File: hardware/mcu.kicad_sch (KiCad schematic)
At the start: 61 parts, among them J1 TYPE-C 16PIN 2MD(073), J2 Conn_ARM_JTAG_SWD_10, J22 Conn_01x16, J3 Conn_02x03_Odd_Even, J4 Conn_02x04_Odd_Even, Q1 DMP1045U-7, Q4 SS8050, Q5 SL1254-3, SW1 MK-12C01-G1.5, SW2 TS-1095PS-A1B2-C3D2, SW3 TS-1095PS-A1B2-C3D2, SW4 10*10*9-6P WX, U1 TPS63031DSK, U10 PY25Q128HA, U2 RP2350A-QFN60, U7 24CS02, Y1 12Mhz

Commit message: prototype v0.3
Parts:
- removed SW4: 10*10*9-6P WX, easyeda2kicad:SW-SMD-6P-L10.5-W10.0_C2858290, symbol easyeda2kicad:10*10*9-6PWX
- added SW5: 7*7*5-6P-L WX, easyeda2kicad:SW-SMD_8P-L7.0-W7.0-P1.40-LS7.4-TL, symbol easyeda2kicad:7*7*5-6P-LWX
- added TP4, TP5: TestPoint, TestPoint:TestPoint_Pad_D1.0mm, symbol Connector:TestPoint
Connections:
- net GND: now also SW5.2 (Public), TP4.1
- net JOY_B: now also U2.33 (GPIO21), SW5.5 (F1); no longer U2.31 (GPIO19)
- net JOY_D: now also SW5.4 (F5)
- net JOY_L: now also U2.31 (GPIO19), SW5.3 (F4); no longer U2.35 (GPIO23)
- net JOY_R: now also SW5.6 (F3)
- net JOY_U: now also U2.35 (GPIO23), SW5.1 (F2); no longer U2.33 (GPIO21)
- net at U2.43 (GPIO29_ADC3): now also TP5.1
- no-connect marks 15 -> 17

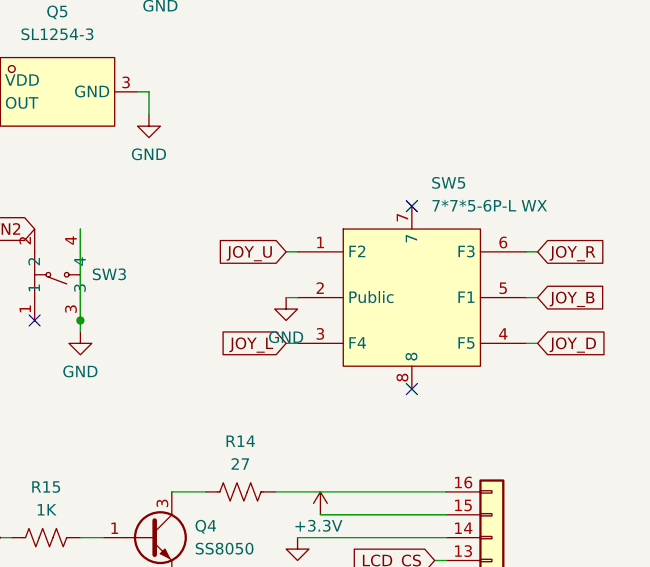
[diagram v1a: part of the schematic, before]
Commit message: Updated joystick
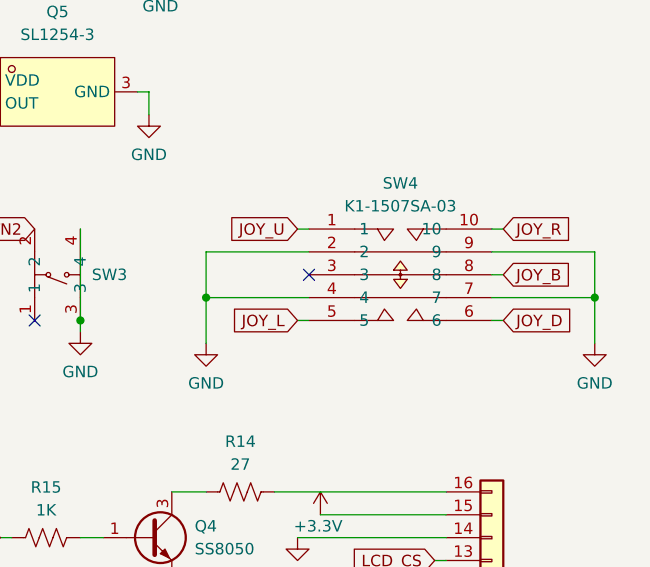
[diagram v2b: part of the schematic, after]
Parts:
- removed SW5: 7*7*5-6P-L WX, easyeda2kicad:SW-SMD_8P-L7.0-W7.0-P1.40-LS7.4-TL, symbol easyeda2kicad:7*7*5-6P-LWX
- added SW4: K1-1507SA-03, easyeda2kicad:KEY-SMD_K1-1507SA-03, symbol easyeda2kicad:K1-1507SA-03
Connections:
- net GND: now also SW4.2, SW4.4, SW4.7, SW4.9
- net JOY_B: now also SW4.8
- net JOY_D: now also SW4.6
- net JOY_L: now also SW4.5
- net JOY_R: now also SW4.10
- net JOY_U: now also SW4.1
- no-connect marks 17 -> 16

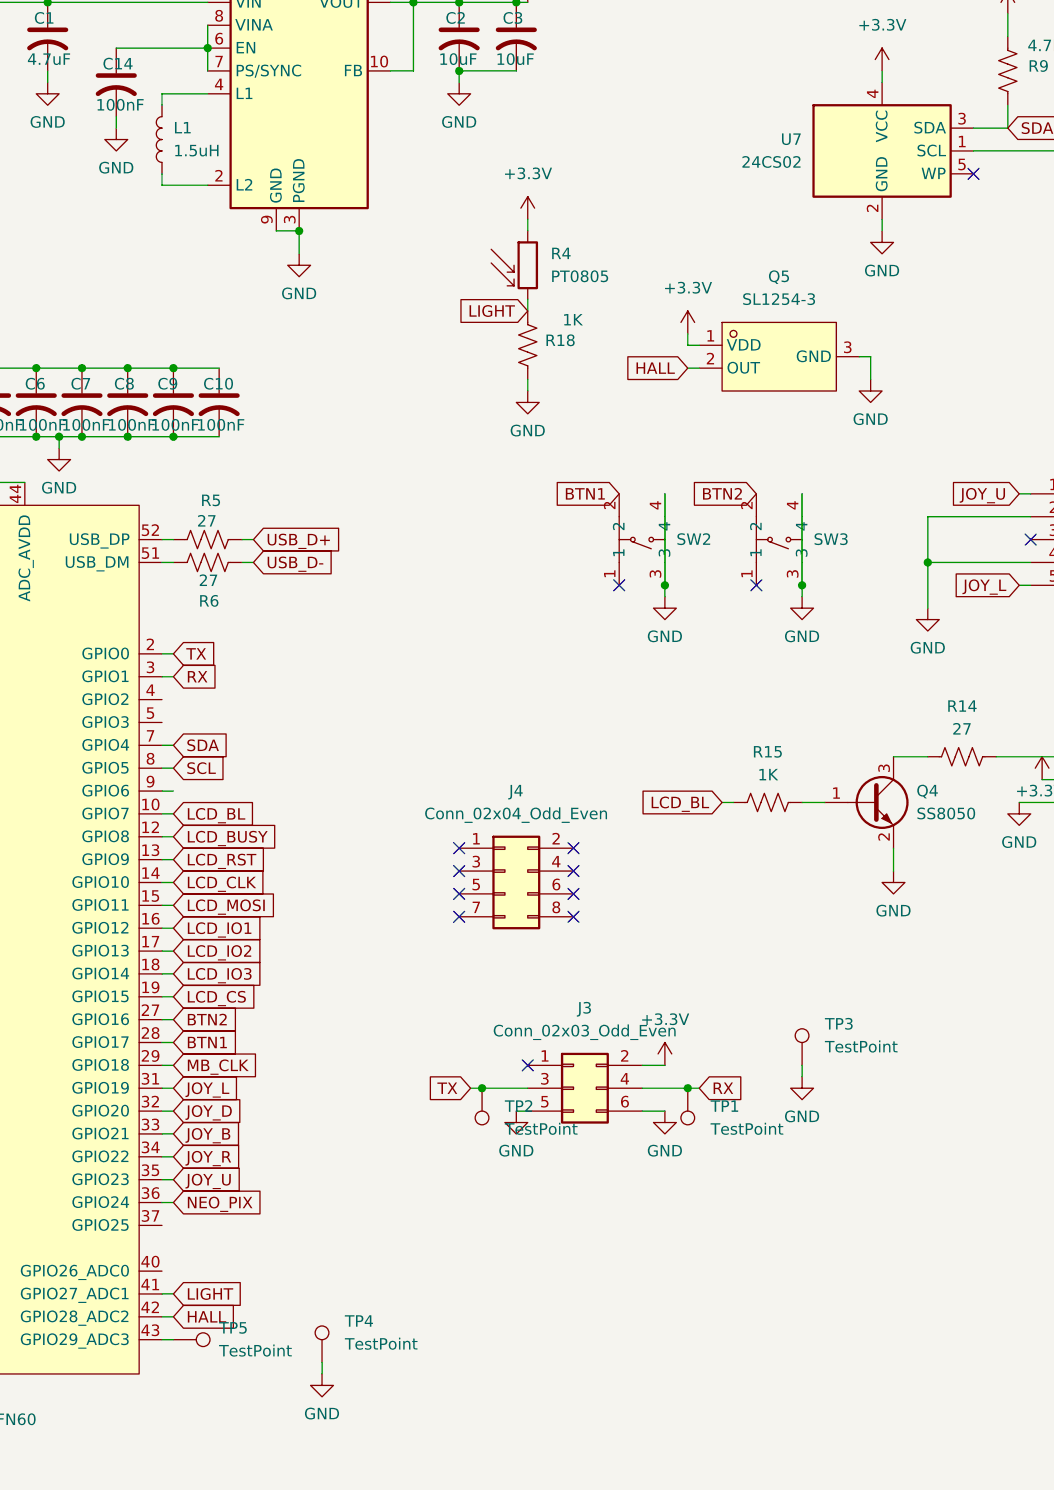
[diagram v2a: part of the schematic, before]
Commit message: Restoring Orion trail
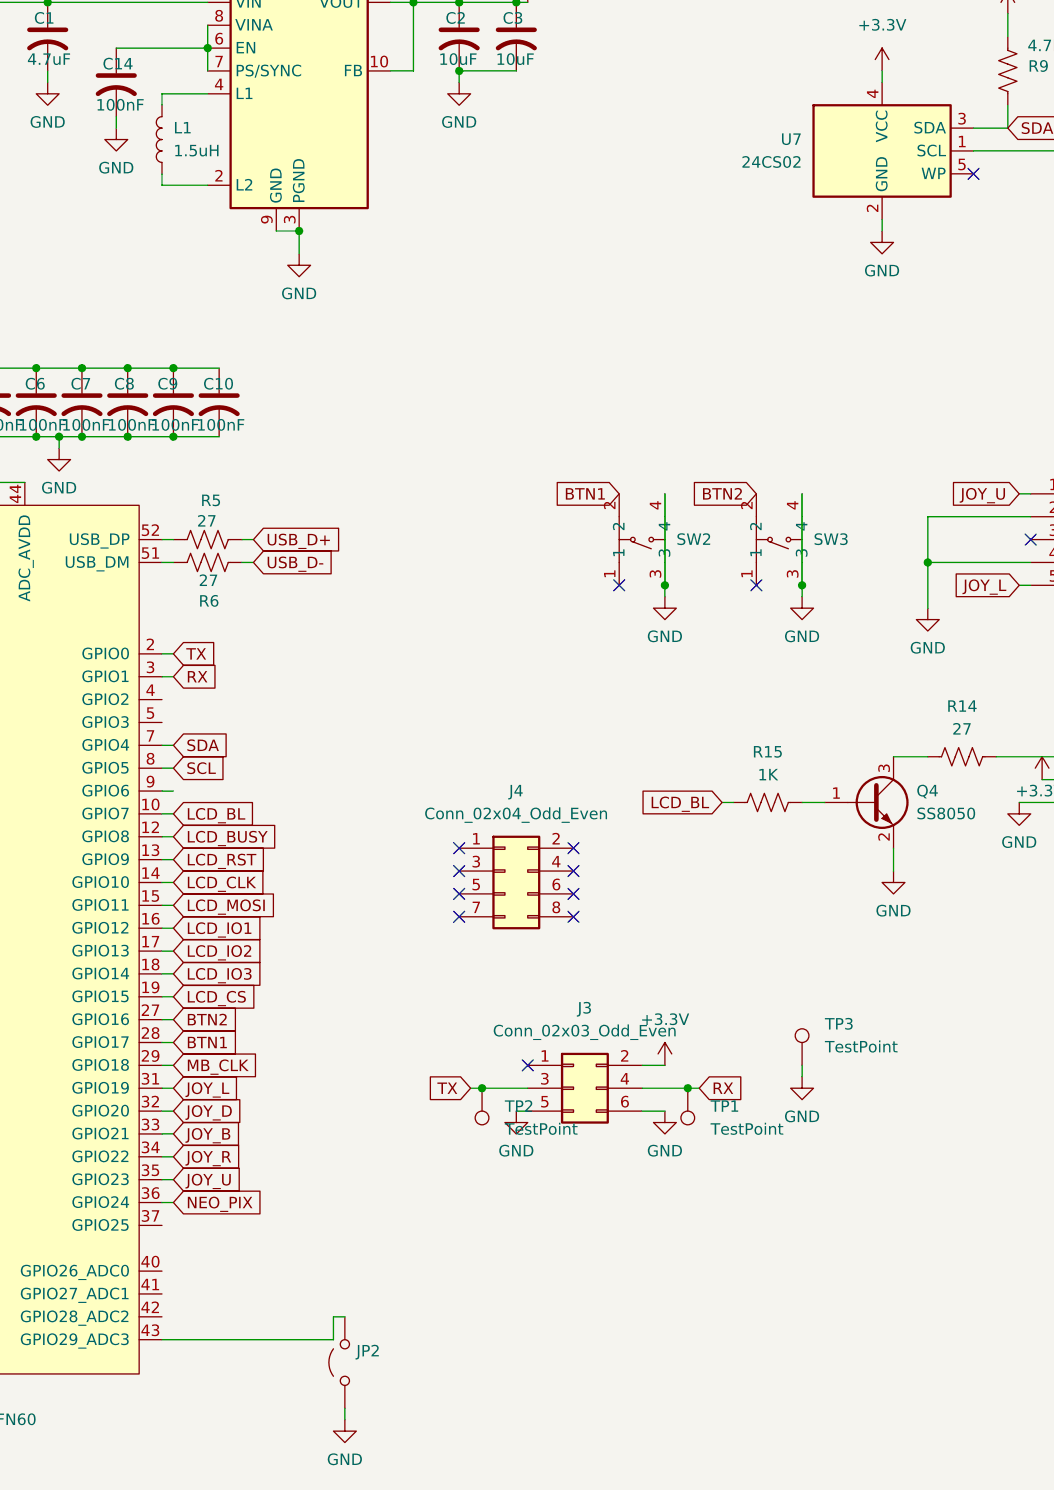
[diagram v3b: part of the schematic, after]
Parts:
- removed Q5: SL1254-3, easyeda2kicad:SOT-23-3_L2.9-W1.3-P1.90-LS2.4-BR, symbol easyeda2kicad:SL1254-3
- removed R18: 1K, Resistor_SMD:R_0603_1608Metric, symbol Device:R_US
- removed R4: PT0805, LED_SMD:LED_0805_2012Metric, symbol Device:R_Photo
- removed TP4, TP5: TestPoint, TestPoint:TestPoint_Pad_D1.0mm, symbol Connector:TestPoint
- added JP2: Jumper_2_Open, Jumper:SolderJumper-2_P1.3mm_Open_RoundedPad1.0x1.5mm, symbol Jumper:Jumper_2_Open
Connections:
- net GND: now also JP2.1 (A)
- net at U2.43 (GPIO29_ADC3): now also JP2.2 (B)
- net HALL: no longer names the net of U2.42 (GPIO28_ADC2)
- net LIGHT: no longer names the net of U2.41 (GPIO27_ADC1)

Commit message: Progress on station communications
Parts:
- J22: footprint easyeda2kicad:CONN-SMD_16P-P0.50_5034801600_1 -> easyeda2kicad:FPC-SMD_16P-P0.50_KH-FPC0.5-H1.0SMT-16P; LCSC Part C2856801 -> C3250117
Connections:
- net GND: now also U7.5 (WP)
- no-connect marks 16 -> 15
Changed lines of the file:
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@@
 	)
 	(junction
+		(at 233.68 58.42)
+		(diameter 0)
+		(color 0 0 0 0)
+	)
+	(junction
 		(at 134.62 87.63)
 		(diameter 0)
@@
 	)
 	(no_connect
-		(at 243.84 53.34)
-	)
-	(no_connect
 		(at 199.39 130.81)
 	)
@@
 	(wire
 		(pts
+			(xy 243.84 58.42) (xy 233.68 58.42)
+		)
+		(stroke
+			(width 0)
+			(type default)
+		)
+	)
+	(wire
+		(pts
 			(xy 49.53 88.9) (xy 64.77 88.9)
 		)
@@
 	(wire
 		(pts
+			(xy 243.84 53.34) (xy 243.84 58.42)
+		)
+		(stroke
+			(width 0)
+			(type default)
+		)
+	)
+	(wire
+		(pts
 			(xy 87.63 142.24) (xy 87.63 146.05)
 		)
@@
 			)
 		)
-		(property "Footprint" "easyeda2kicad:CONN-SMD_16P-P0.50_5034801600_1"
+		(property "Footprint" "easyeda2kicad:FPC-SMD_16P-P0.50_KH-FPC0.5-H1.0SMT-16P"
 			(at 270.51 138.43 0)
 			(hide yes)
@@
 			)
 		)
-		(property "LCSC Part" "C2856801"
+		(property "LCSC Part" "C3250117"
 			(at 270.51 138.43 0)
 			(hide yes)
